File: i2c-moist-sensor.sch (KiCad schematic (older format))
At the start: 21 parts, among them IC1 ATTINY441-SSU, P1 CONN_02X03, X1 16MHz

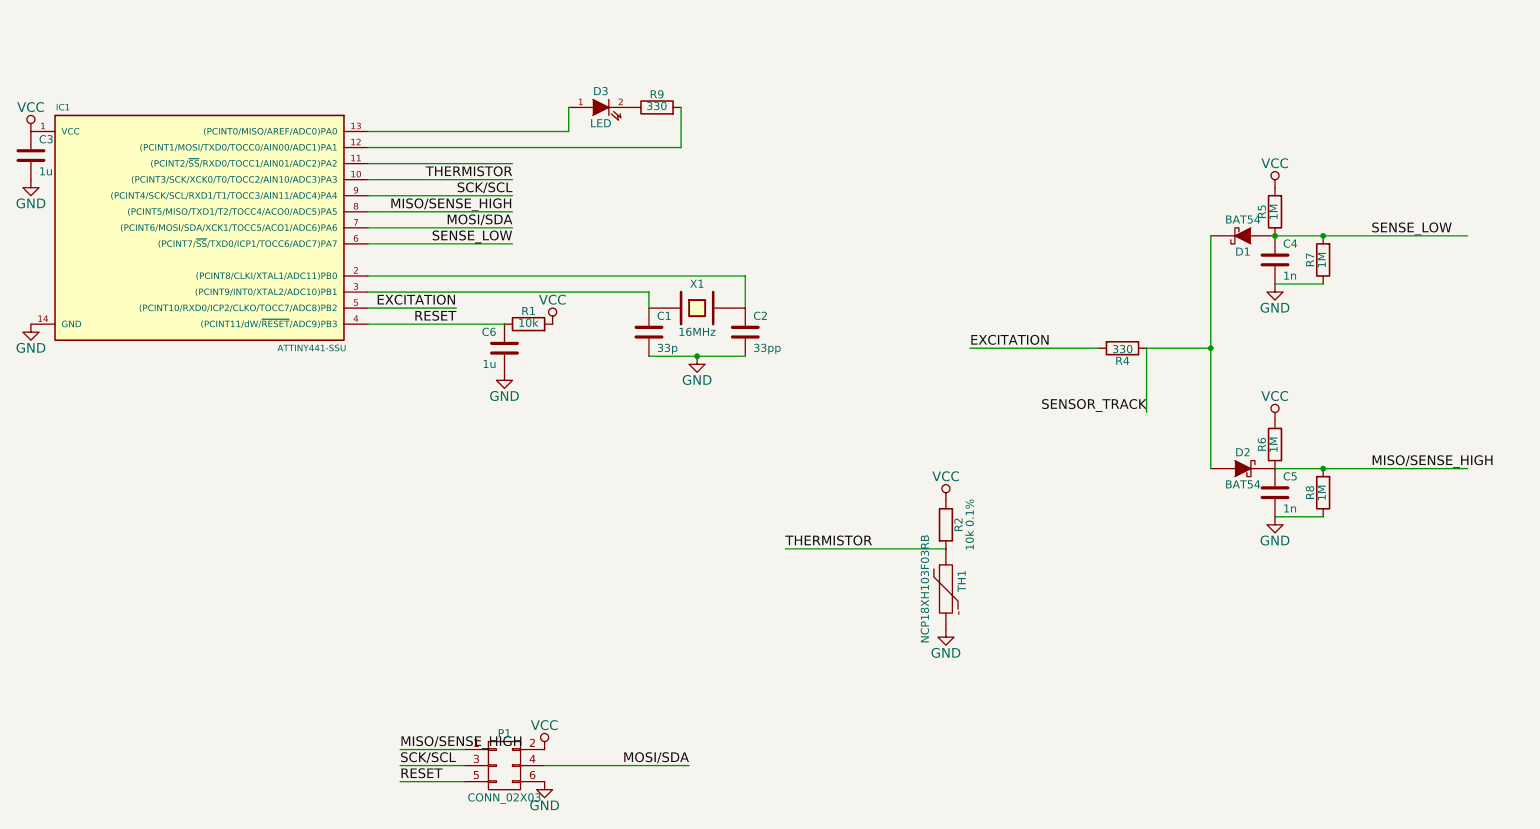
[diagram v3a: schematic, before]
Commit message: Power thermistor and moisture sensing circuitry from a pin rather than directly so lower the power consumption
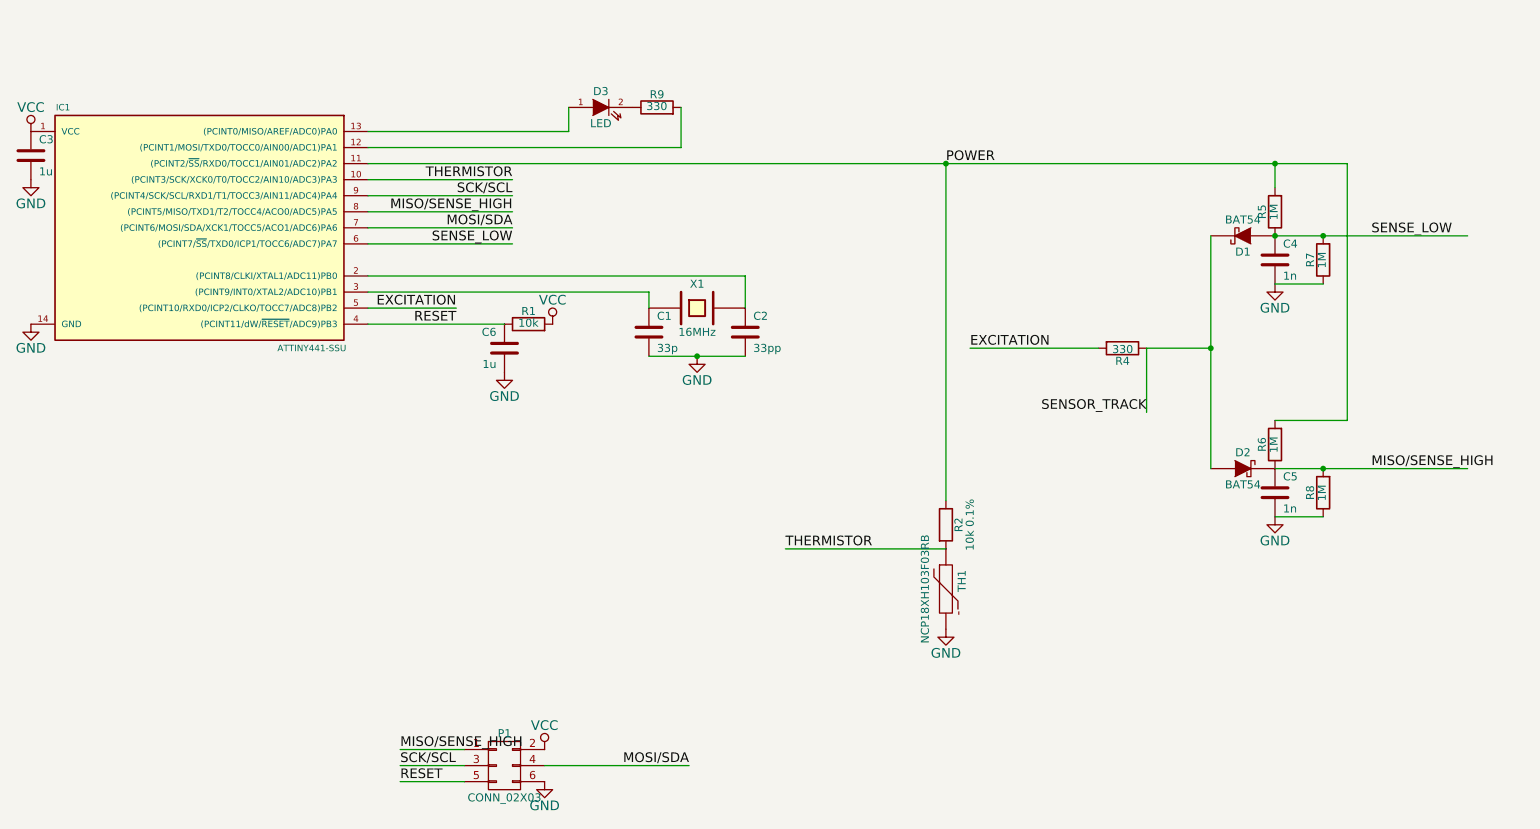
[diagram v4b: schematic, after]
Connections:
- net labels added: POWER
- wire segments 30 -> 34
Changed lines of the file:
@@
 LIBS:valves
 LIBS:i2c-moist-sensor-cache
-EELAYER 25 0
+EELAYER 26 0
 EELAYER END
 $Descr A4 11693 8268
@@
 $EndComp
 $Comp
-L VCC #PWR05
-U 1 1 54D2215E
-P 9300 2050
-F 0 "#PWR05" H 9300 1900 60  0001 C CNN
-F 1 "VCC" H 9300 2200 60  0000 C CNN
-F 2 "" H 9300 2050 60  0000 C CNN
-F 3 "" H 9300 2050 60  0000 C CNN
-	1    9300 2050
-	1    0    0    -1
-$EndComp
-$Comp
 L R R5
 U 1 1 54D22174
@@
 	1    9300 3650
 	-1   0    0    1
-$EndComp
-$Comp
-L VCC #PWR08
-U 1 1 54D226D9
-P 9300 3500
-F 0 "#PWR08" H 9300 3350 60  0001 C CNN
-F 1 "VCC" H 9300 3650 60  0000 C CNN
-F 2 "" H 9300 3500 60  0000 C CNN
-F 3 "" H 9300 3500 60  0000 C CNN
-	1    9300 3500
-	1    0    0    -1
 $EndComp
 Text Label 9900 3800 0    60   ~ 0
@@
 	1    0    0    -1
 $EndComp
-$Comp
-L VCC #PWR013
-U 1 1 54E060B0
-P 7250 4000
-F 0 "#PWR013" H 7250 3850 60  0001 C CNN
-F 1 "VCC" H 7250 4150 60  0000 C CNN
-F 2 "" H 7250 4000 60  0000 C CNN
-F 3 "" H 7250 4000 60  0000 C CNN
-	1    7250 4000
-	1    0    0    -1
-$EndComp
 Text Label 6250 4300 0    60   ~ 0
 THERMISTOR
@@
 Connection ~ 9300 2350
 Wire Wire Line
-	3650 1900 4550 1900
+	3650 1900 9750 1900
 Wire Wire Line
 	5600 1800 3650 1800
@@
 	1    0    0    -1
 $EndComp
+Wire Wire Line
+	9300 1900 9300 2050
+Wire Wire Line
+	9300 3500 9750 3500
+Wire Wire Line
+	9750 3500 9750 1900
+Connection ~ 9300 1900
+Wire Wire Line
+	7250 4000 7250 1900
+Connection ~ 7250 1900
+Text Label 7250 1900 0    60   ~ 0
+POWER
 $EndSCHEMATC
